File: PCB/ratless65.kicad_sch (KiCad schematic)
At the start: 132 parts, among them U1 ProMicro, U2 ProMicro

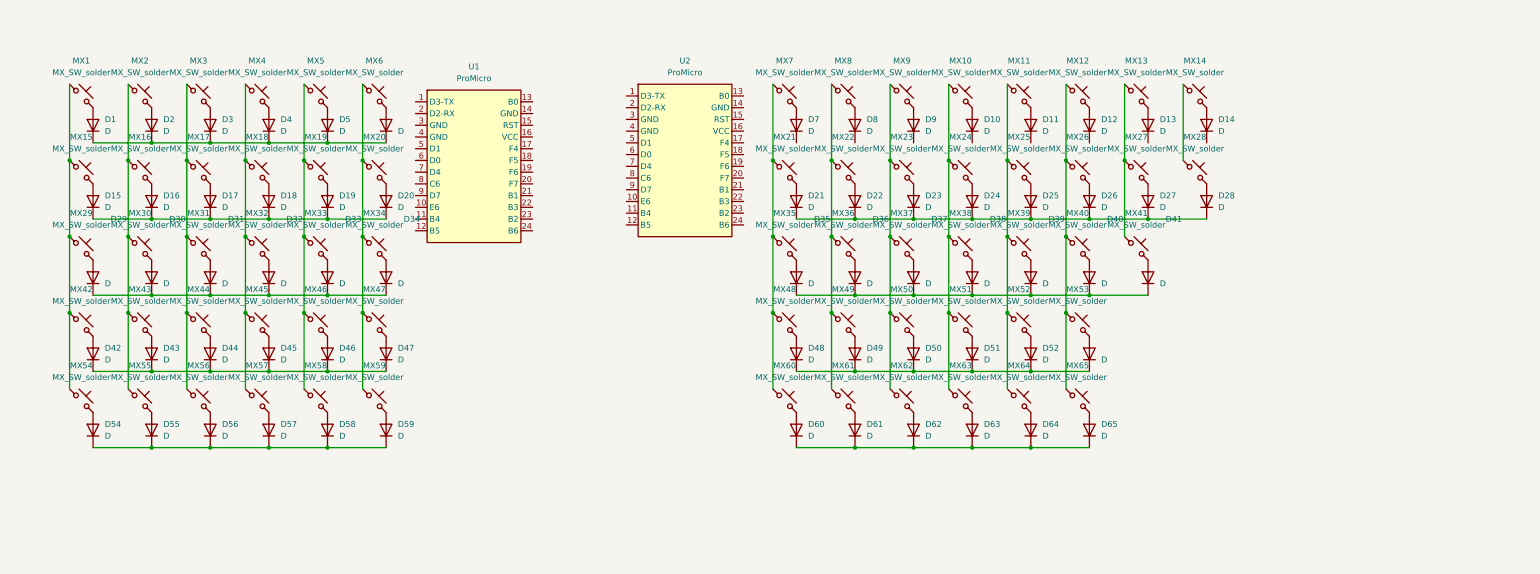
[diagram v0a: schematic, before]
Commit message: Started wiring to the MCUs + Added TRRS jacks + Lots...
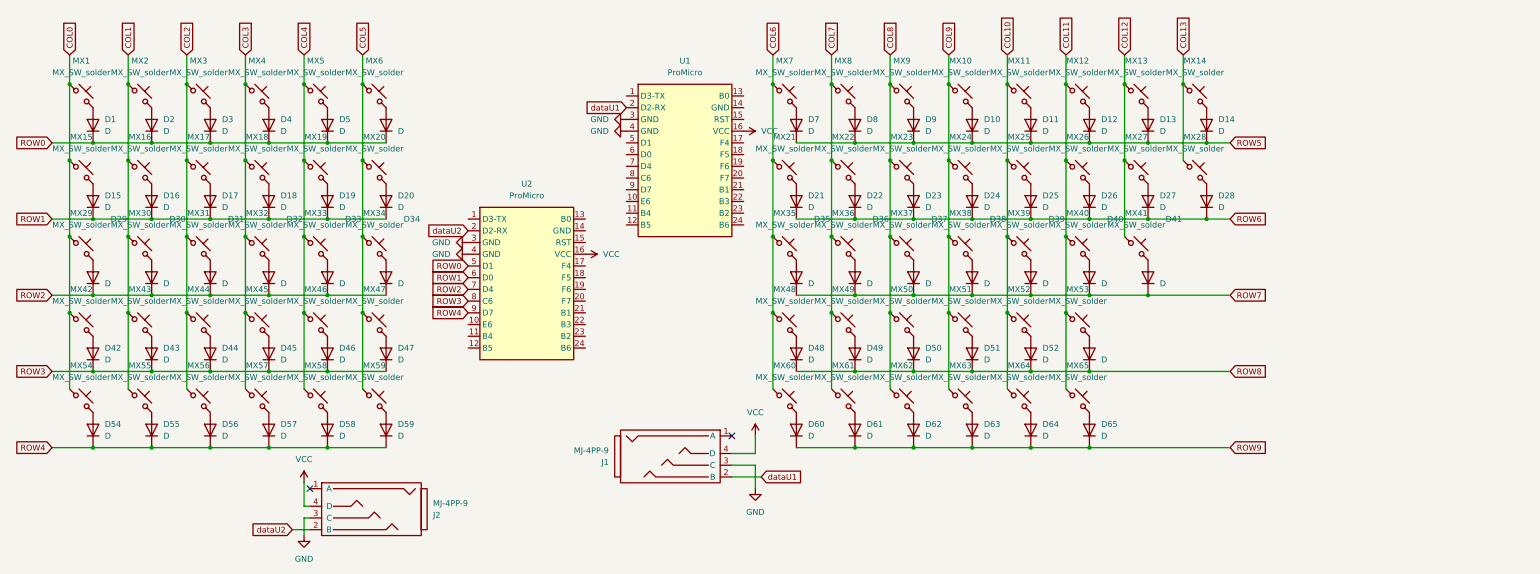
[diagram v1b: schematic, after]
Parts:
- added J1, J2: MJ-4PP-9, MJ-4PP-9:MJ-4PP-9, symbol trrs_keyboard:MJ-4PP-9
- MX41, MX53: footprint PCM_marbastlib-mx:SW_MX_1u -> PCM_marbastlib-mx:SW_MX_1.5u
- renumbered U2 to U1, U1 to U2
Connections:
- net ROW4: now reaches D54.1 (K), D55.1 (K), D56.1 (K), D57.1 (K), D58.1 (K), D59.1 (K)
- net ROW4: now also U2.9 (D7)
- net COL8: now reaches MX23.1, MX37.1, MX50.1, MX62.1, MX9.1
- net ROW8: now reaches D48.1 (K), D49.1 (K), D50.1 (K), D51.1 (K), D52.1 (K), D53.1 (K)
- net ROW6: now reaches D21.1 (K), D22.1 (K), D23.1 (K), D24.1 (K), D25.1 (K), D26.1 (K), D27.1 (K), D28.1 (K)
- net COL11: now reaches MX12.1, MX26.1, MX40.1, MX53.1, MX65.1
- net ROW0: now reaches D1.1 (K), D2.1 (K), D3.1 (K), D4.1 (K), D5.1 (K), D6.1 (K)
- net ROW0: now also U2.5 (D1)
- net ROW3: now reaches D42.1 (K), D43.1 (K), D44.1 (K), D45.1 (K), D46.1 (K), D47.1 (K)
- net ROW3: now also U2.8 (C6)
- net ROW1: now reaches D15.1 (K), D16.1 (K), D17.1 (K), D18.1 (K), D19.1 (K), D20.1 (K)
- net ROW1: now also U2.6 (D0)
- net COL6: now reaches MX21.1, MX35.1, MX48.1, MX60.1, MX7.1
- net ROW7: now reaches D35.1 (K), D36.1 (K), D37.1 (K), D38.1 (K), D39.1 (K), D40.1 (K), D41.1 (K)
- net COL1: now reaches MX16.1, MX2.1, MX30.1, MX43.1, MX55.1
- net ROW2: now reaches D29.1 (K), D30.1 (K), D31.1 (K), D32.1 (K), D33.1 (K), D34.1 (K)
- net ROW2: now also U2.7 (D4)
- net ROW9: now reaches D60.1 (K), D61.1 (K), D62.1 (K), D63.1 (K), D64.1 (K), D65.1 (K)
- net COL3: now reaches MX18.1, MX32.1, MX4.1, MX45.1, MX57.1
- net COL12: now reaches MX13.1, MX27.1, MX41.1
- net COL9: now reaches MX10.1, MX24.1, MX38.1, MX51.1, MX63.1
- net COL0: now reaches MX1.1, MX15.1, MX29.1, MX42.1, MX54.1
- net ROW5: now reaches D7.1 (K)
- net ROW5: now also D10.1 (K), D11.1 (K), D12.1 (K), D13.1 (K), D14.1 (K), D8.1 (K), D9.1 (K)
- net COL5: now reaches MX20.1, MX34.1, MX47.1, MX59.1, MX6.1
- net COL7: now reaches MX22.1, MX36.1, MX49.1, MX61.1, MX8.1
- net COL10: now reaches MX11.1, MX25.1, MX39.1, MX52.1, MX64.1
- net COL2: now reaches MX17.1, MX3.1, MX31.1, MX44.1, MX56.1
- net COL4: now reaches MX19.1, MX33.1, MX46.1, MX5.1, MX58.1
- net COL13: now reaches MX14.1, MX28.1
- net VCC: now reaches U1.16 (VCC)
- net VCC: now also U2.16 (VCC), J1.4 (D), J2.4 (D)
- net dataU1: now reaches U1.2 (D2-RX)
- net dataU1: now also J1.2 (B)
- net GND: now reaches U1.3 (GND)
- net GND: now also U1.4 (GND), U2.3 (GND), U2.4 (GND), J1.3 (C), J2.3 (C)
- net dataU2: now reaches U2.2 (D2-RX)
- net dataU2: now also J2.2 (B)
- no-connect marks 0 -> 2
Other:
- moved on the sheet: U2

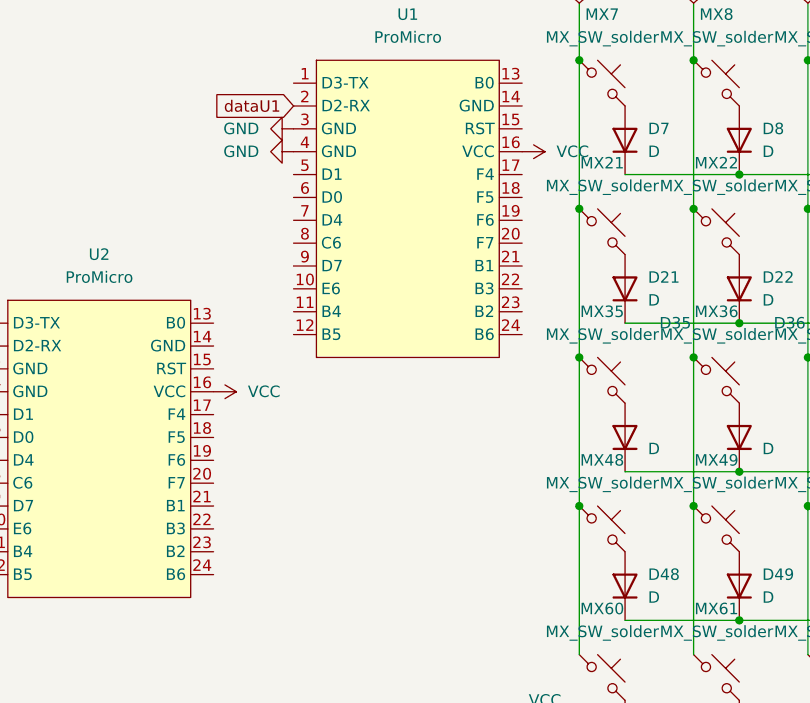
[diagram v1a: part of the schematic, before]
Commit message: Finished PCB, need to add resistors for I2C
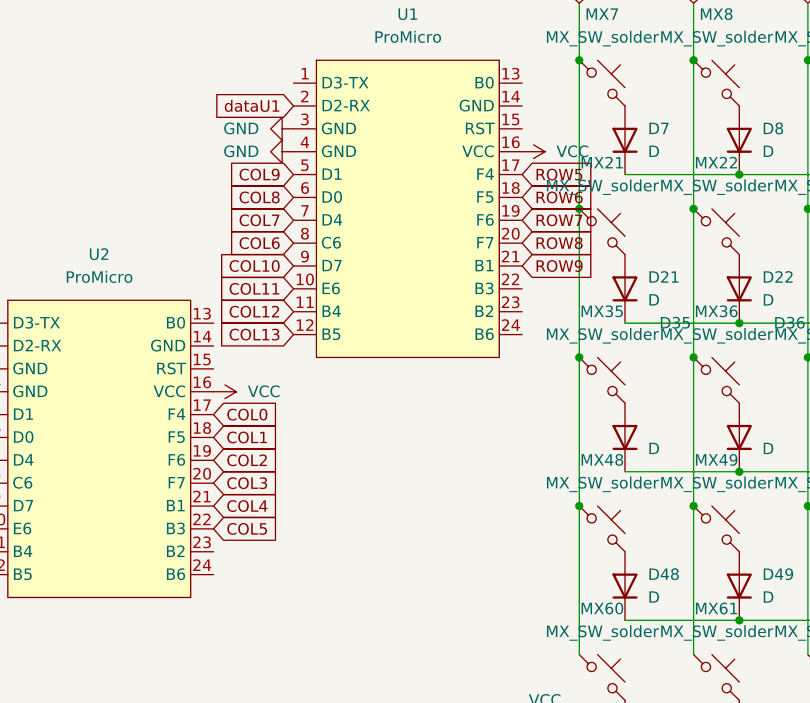
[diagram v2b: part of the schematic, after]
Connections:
- net COL0: now also U2.17 (F4)
- net COL1: now also U2.18 (F5)
- net COL10: now also U1.9 (D7)
- net COL11: now also U1.10 (E6)
- net COL12: now also U1.11 (B4)
- net COL13: now also U1.12 (B5)
- net COL2: now also U2.19 (F6)
- net COL3: now also U2.20 (F7)
- net COL4: now also U2.21 (B1)
- net COL5: now also U2.22 (B3)
- net COL6: now also U1.8 (C6)
- net COL7: now also U1.7 (D4)
- net COL8: now also U1.6 (D0)
- net COL9: now also U1.5 (D1)
- net ROW5: now also U1.17 (F4)
- net ROW6: now also U1.18 (F5)
- net ROW7: now also U1.19 (F6)
- net ROW8: now also U1.20 (F7)
- net ROW9: now also U1.21 (B1)

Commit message: I have no clue what changed but just want everything synced
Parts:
- added R1, R2: 4.7k, PCM_Resistor_SMD_AKL:R_1206_3216Metric, symbol Device:R
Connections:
- net COL0: now also U2.5 (D1); no longer U2.17 (F4)
- net COL1: now also U2.6 (D0); no longer U2.18 (F5)
- net COL2: now also U2.7 (D4); no longer U2.19 (F6)
- net COL3: now also U2.8 (C6); no longer U2.20 (F7)
- net COL4: now also U2.9 (D7); no longer U2.21 (B1)
- net COL5: now also U2.10 (E6); no longer U2.22 (B3)
- net COL6: now also U1.5 (D1); no longer U1.8 (C6)
- net COL7: now also U1.6 (D0); no longer U1.7 (D4)
- net COL8: now also U1.7 (D4); no longer U1.6 (D0)
- net COL9: now also U1.8 (C6); no longer U1.5 (D1)
- net GND: now also R2.2
- net ROW0: now also U2.17 (F4); no longer U2.5 (D1)
- net ROW1: now also U2.18 (F5); no longer U2.6 (D0)
- net ROW2: now also U2.19 (F6); no longer U2.7 (D4)
- net ROW3: now also U2.20 (F7); no longer U2.8 (C6)
- net ROW4: now also U2.21 (B1); no longer U2.9 (D7)
- net VCC: now also R1.2
- net at U1.24 (B6): now also R2.1
- net at U2.24 (B6): now also R1.1
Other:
- moved on the sheet: D1, D10, D11, D12, D13, D14, D15, D16, D17, D18, D19, D2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
